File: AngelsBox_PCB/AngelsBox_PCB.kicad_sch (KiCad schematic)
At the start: 37 parts

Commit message: first pcb commit
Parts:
- removed D1, D10, D11, D12, D13, D14, D15, D16, D17, D18, D2, D3, D4, D5, D6, D7, D8, D9: D_Small, Diode_SMD:D_SOD-123, symbol Device:D_Small
- MX16, MX17, MX18: footprint AngelBox_Switch_Library:Kailh_Choc-CircleDesign -> Kailh_Choc:KailhChoc-1U
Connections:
- net ROW2 is gone; now on net COL14: U1.1 (GP1)
- net ROW3 is gone; now on net COL15: U1.28 (GP28)
- net COL0: now also U1.15 (GP15); no longer U1.26 (GP26)
- net COL1: now also U1.14 (GP14); no longer U1.15 (GP15)
- net COL10: now also U1.5 (GP5); no longer U1.6 (GP6)
- net COL11: now also U1.4 (GP4); no longer U1.5 (GP5)
- net COL12: now also U1.3 (GP3); no longer U1.4 (GP4)
- net COL13: now also U1.2 (GP2); no longer U1.3 (GP3)
- net COL14: no longer U1.2 (GP2)
- net COL15: no longer MX17.1 (COL), MX18.1 (COL), U1.27 (GP27)
- net COL2: now also U1.13 (GP13); no longer U1.14 (GP14)
- net COL3: now also U1.12 (GP12); no longer U1.13 (GP13)
- net COL4: now also U1.11 (GP11); no longer U1.12 (GP12)
- net COL5: now also U1.10 (GP10); no longer U1.11 (GP11)
- net COL6: now also U1.9 (GP9); no longer U1.10 (GP10)
- net COL7: now also U1.8 (GP8); no longer U1.9 (GP9)
- net COL8: now also U1.7 (GP7); no longer U1.8 (GP8)
- net COL9: now also U1.6 (GP6); no longer U1.7 (GP7)
- net ROW0: now also MX1.2 (ROW), MX16.2 (ROW), MX17.2 (ROW), MX18.2 (ROW), MX2.2 (ROW), MX3.2 (ROW), MX4.2 (ROW), MX5.2 (ROW)
- net ROW1: now also MX10.2 (ROW), MX11.2 (ROW), MX12.2 (ROW), MX13.2 (ROW), MX14.2 (ROW), MX15.2 (ROW), MX6.2 (ROW), MX7.2 (ROW), MX8.2 (ROW), MX9.2 (ROW)
- new net COL16: MX17.1 (COL), U1.27 (GP27)
- new net COL17: MX18.1 (COL), U1.26 (GP26)
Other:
- moved on the sheet: MX16, MX17, MX18

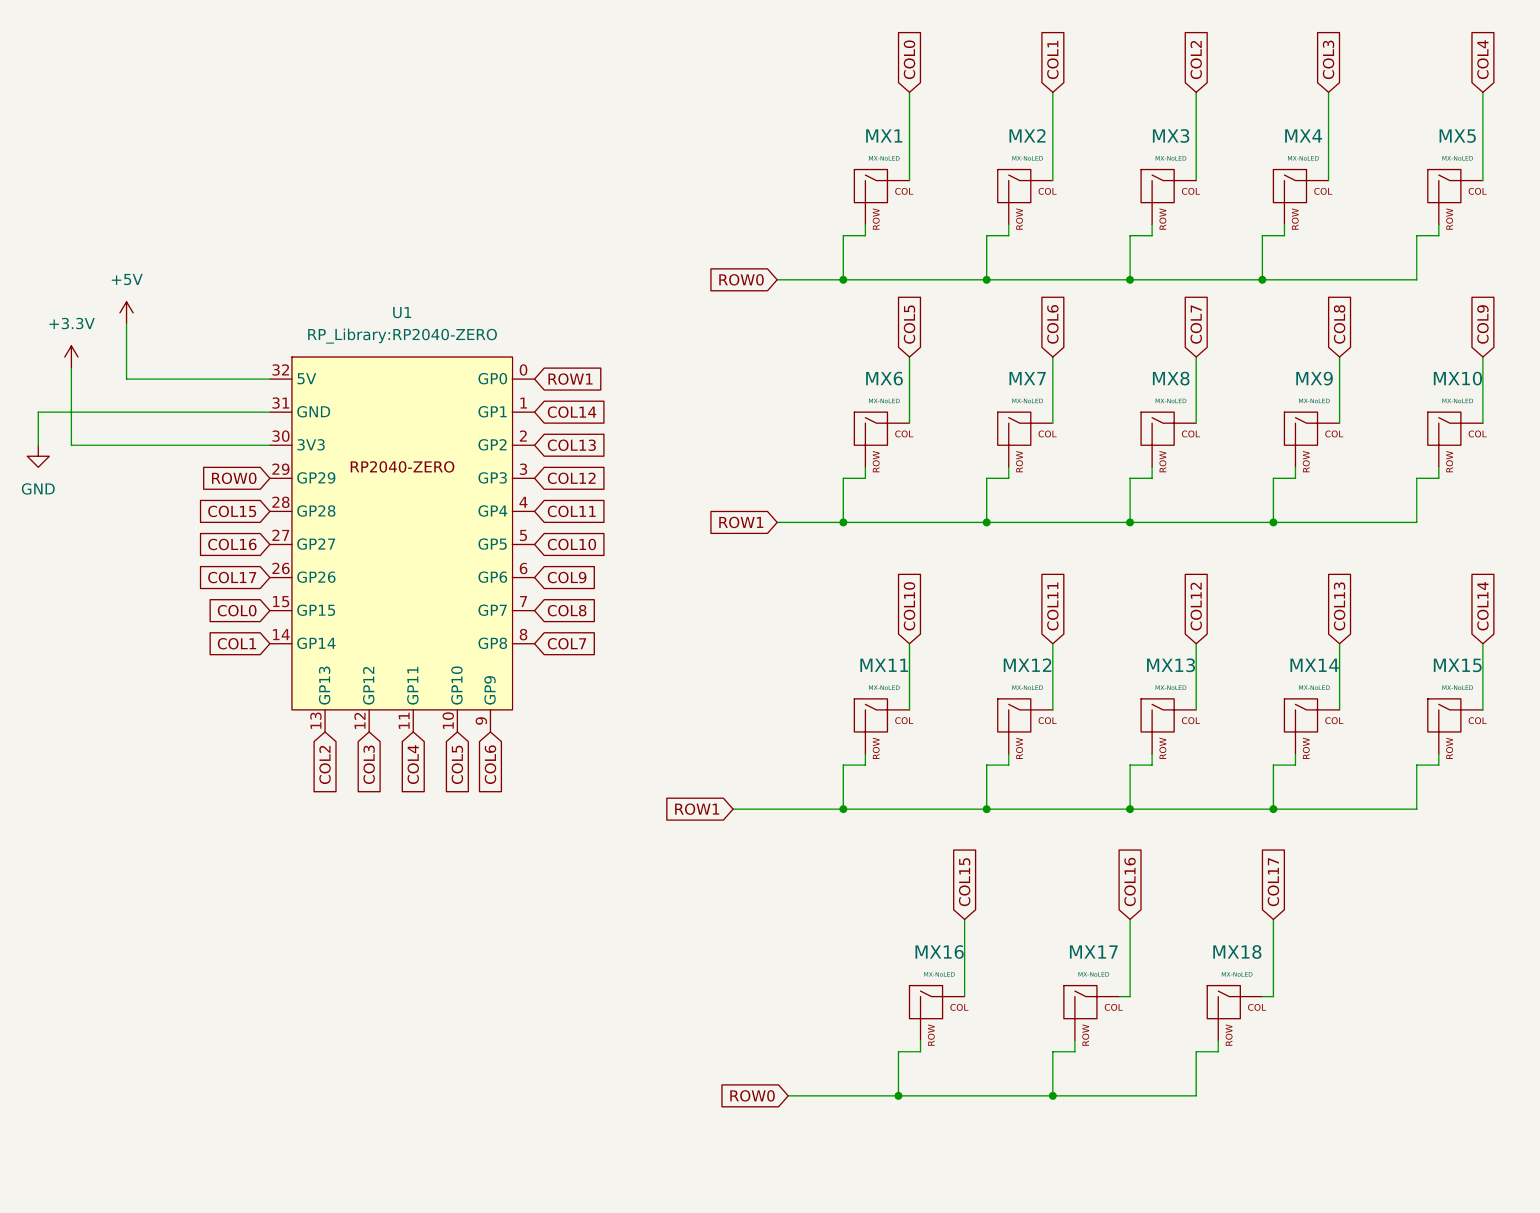
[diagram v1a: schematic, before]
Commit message: Version 1.0 Adds first completed pcb. Adds Gerber files for pcb. Adds 3d stl models for the pcb and first version of keycaps.
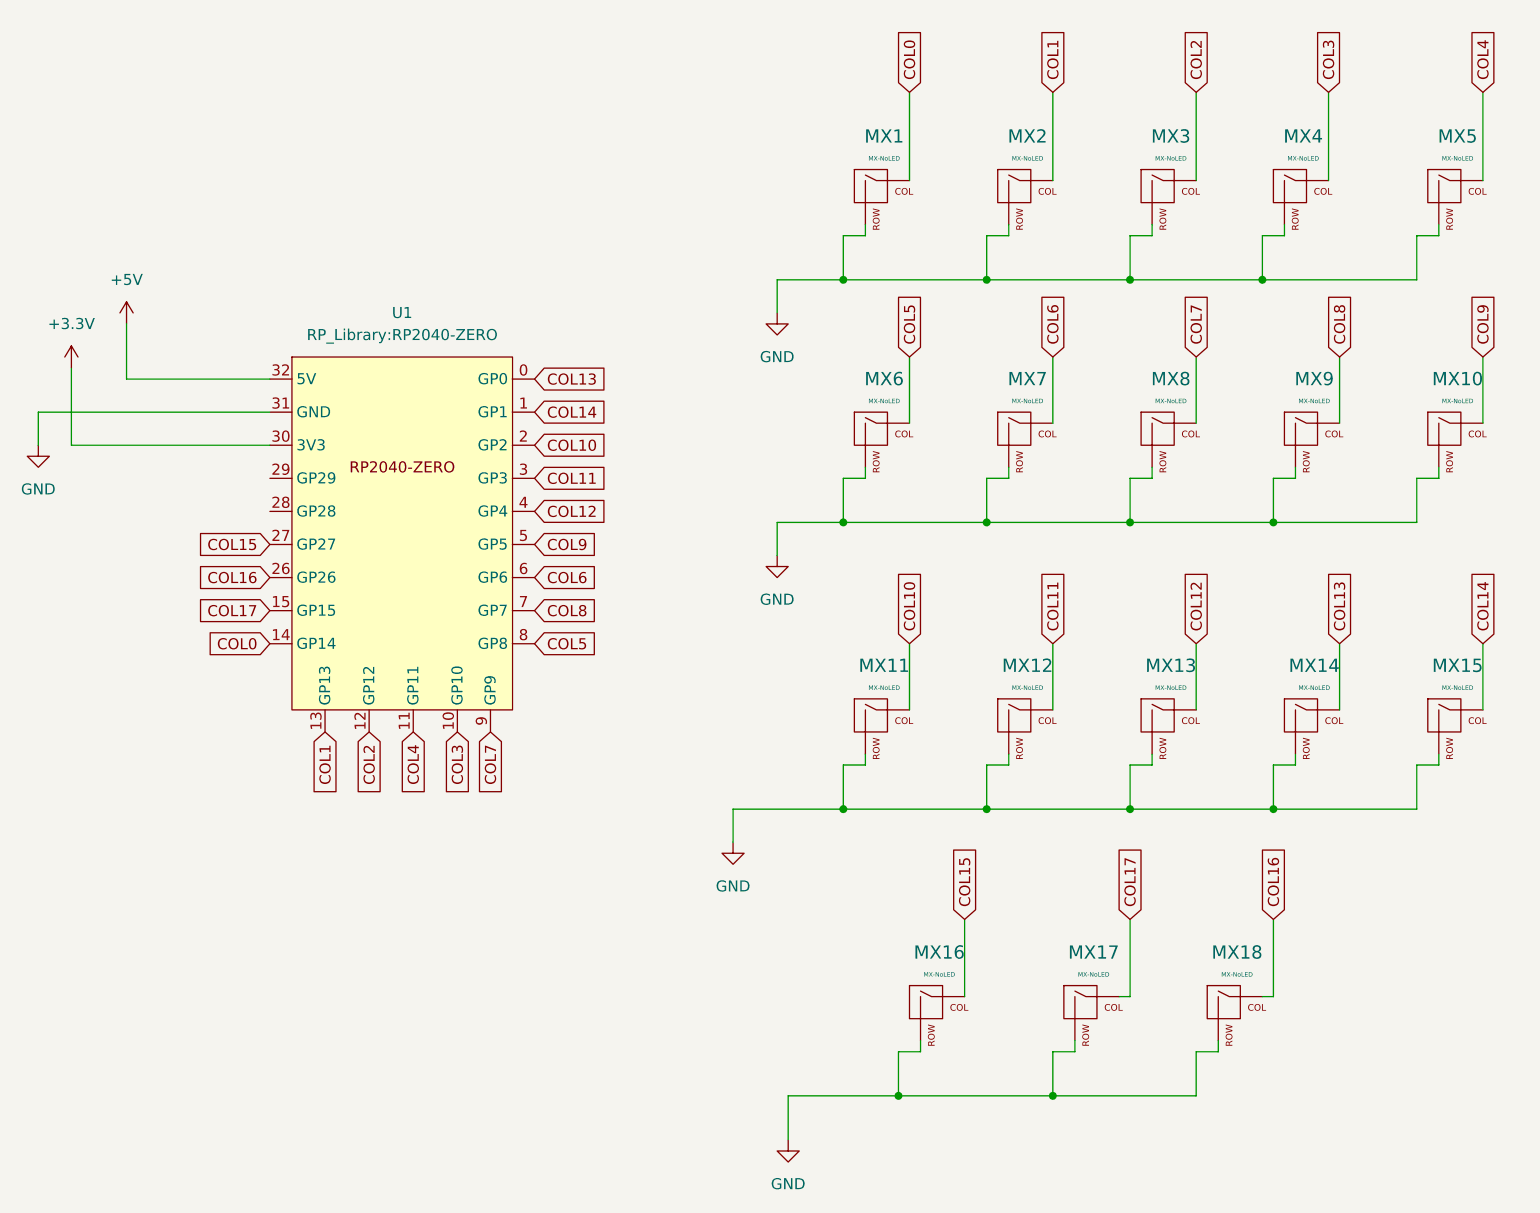
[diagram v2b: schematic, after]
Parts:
- MX1, MX10, MX11, MX12, MX13, MX14, MX15, MX2, MX3, MX4, MX5, MX6, MX7, MX8, MX9: footprint AngelBox_Switch_Library:Kailh_Choc-CircleDesign -> AngelBox_Switch_Library:Kailh_Choc_Hotswap-CircleDesign
- MX16, MX17, MX18: footprint Kailh_Choc:KailhChoc-1U -> AngelBox_Switch_Library:KailhChoc-1U-Hotswap
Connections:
- net COL0: now also U1.14 (GP14); no longer U1.15 (GP15)
- net COL1: now also U1.13 (GP13); no longer U1.14 (GP14)
- net COL10: now also U1.2 (GP2); no longer U1.5 (GP5)
- net COL11: now also U1.3 (GP3); no longer U1.4 (GP4)
- net COL12: now also U1.4 (GP4); no longer U1.3 (GP3)
- net COL13: now also U1.0 (GP0); no longer U1.2 (GP2)
- net COL15: now also U1.27 (GP27); no longer U1.28 (GP28)
- net COL16: now also MX18.1 (COL), U1.26 (GP26); no longer MX17.1 (COL), U1.27 (GP27)
- net COL17: now also MX17.1 (COL), U1.15 (GP15); no longer MX18.1 (COL), U1.26 (GP26)
- net COL2: now also U1.12 (GP12); no longer U1.13 (GP13)
- net COL3: now also U1.10 (GP10); no longer U1.12 (GP12)
- net COL5: now also U1.8 (GP8); no longer U1.10 (GP10)
- net COL6: now also U1.6 (GP6); no longer U1.9 (GP9)
- net COL7: now also U1.9 (GP9); no longer U1.8 (GP8)
- net COL9: now also U1.5 (GP5); no longer U1.6 (GP6)
- net GND: now also MX1.2 (ROW), MX10.2 (ROW), MX11.2 (ROW), MX12.2 (ROW), MX13.2 (ROW), MX14.2 (ROW), MX15.2 (ROW), MX16.2 (ROW), MX17.2 (ROW), MX18.2 (ROW), MX2.2 (ROW), MX3.2 (ROW), MX4.2 (ROW), MX5.2 (ROW), MX6.2 (ROW), MX7.2 (ROW), MX8.2 (ROW), MX9.2 (ROW)
- removed net ROW0: MX1.2 (ROW), MX16.2 (ROW), MX17.2 (ROW), MX18.2 (ROW), MX2.2 (ROW), MX3.2 (ROW), MX4.2 (ROW), MX5.2 (ROW), U1.29 (GP29)
- removed net ROW1: MX10.2 (ROW), MX11.2 (ROW), MX12.2 (ROW), MX13.2 (ROW), MX14.2 (ROW), MX15.2 (ROW), MX6.2 (ROW), MX7.2 (ROW), MX8.2 (ROW), MX9.2 (ROW), U1.0 (GP0)
